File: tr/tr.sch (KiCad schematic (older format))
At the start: 104 parts, among them J1 SMA, J2 SMA, J3 SMA, K1 CONN_3, Q1 Si7850, Q3 STD2NK90ZT4, Q4 STD2NK90ZT4, T1 DA2033-AL_, U1 L6388E, U2 LT1631, U3 LT3757

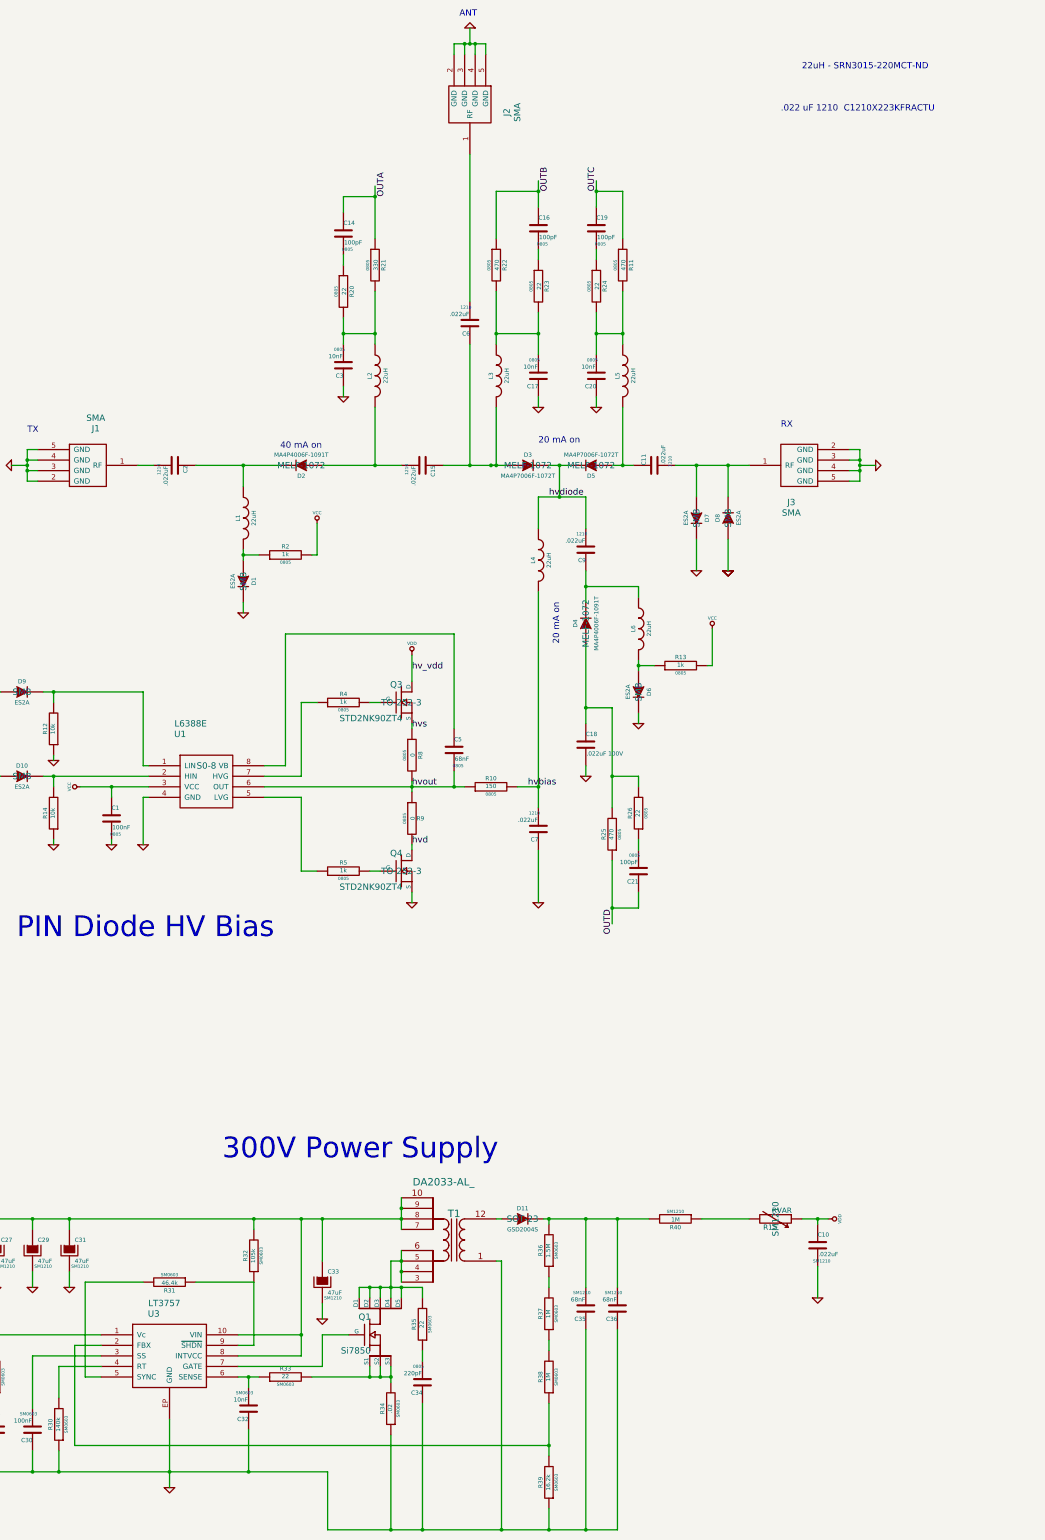
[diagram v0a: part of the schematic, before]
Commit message: routing for high voltage power supply
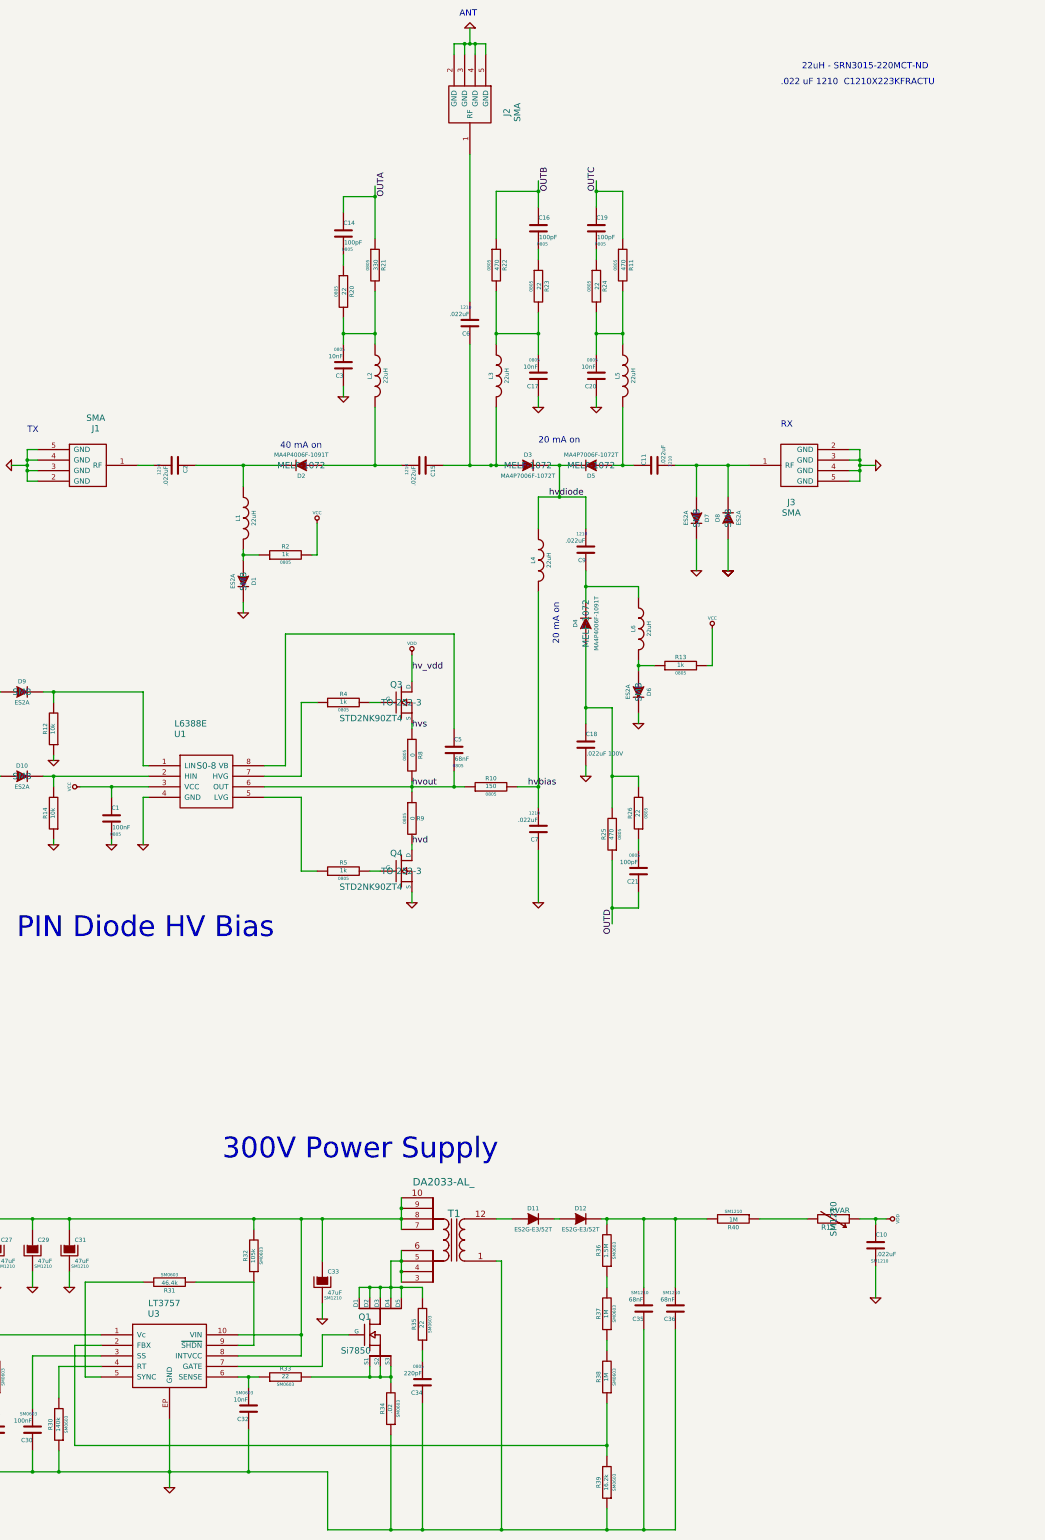
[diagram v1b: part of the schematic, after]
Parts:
- added D12: ES2G-E3/52T, ~, symbol DIODE
- D11: value GSD2004S -> ES2G-E3/52T; footprint SOT-23 -> ~
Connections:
- wire segments 255 -> 256
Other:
- moved on the sheet: C10, C35, C36, R15, R36, R37, R38, R39, R40

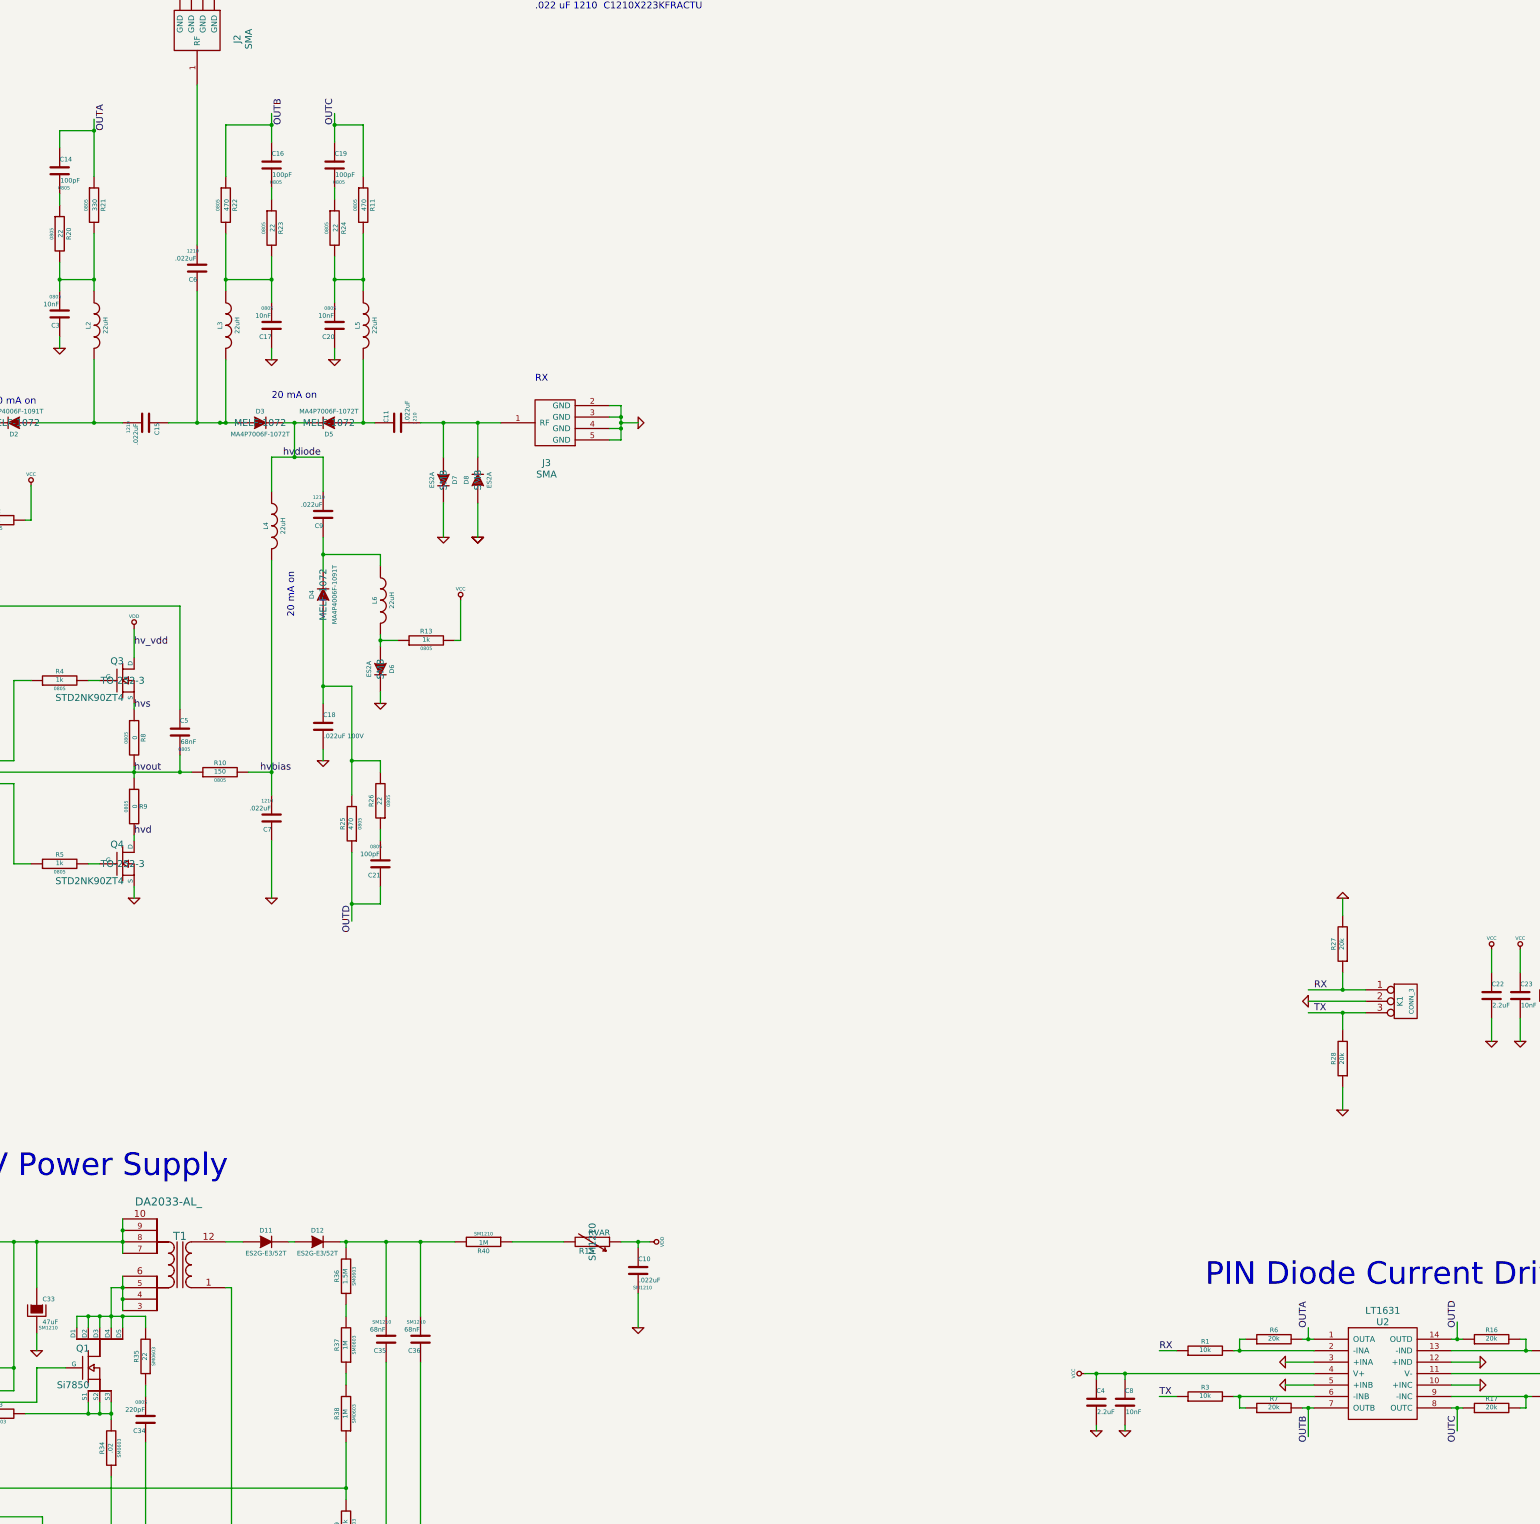
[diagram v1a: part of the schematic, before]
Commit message: work on transmitter layout
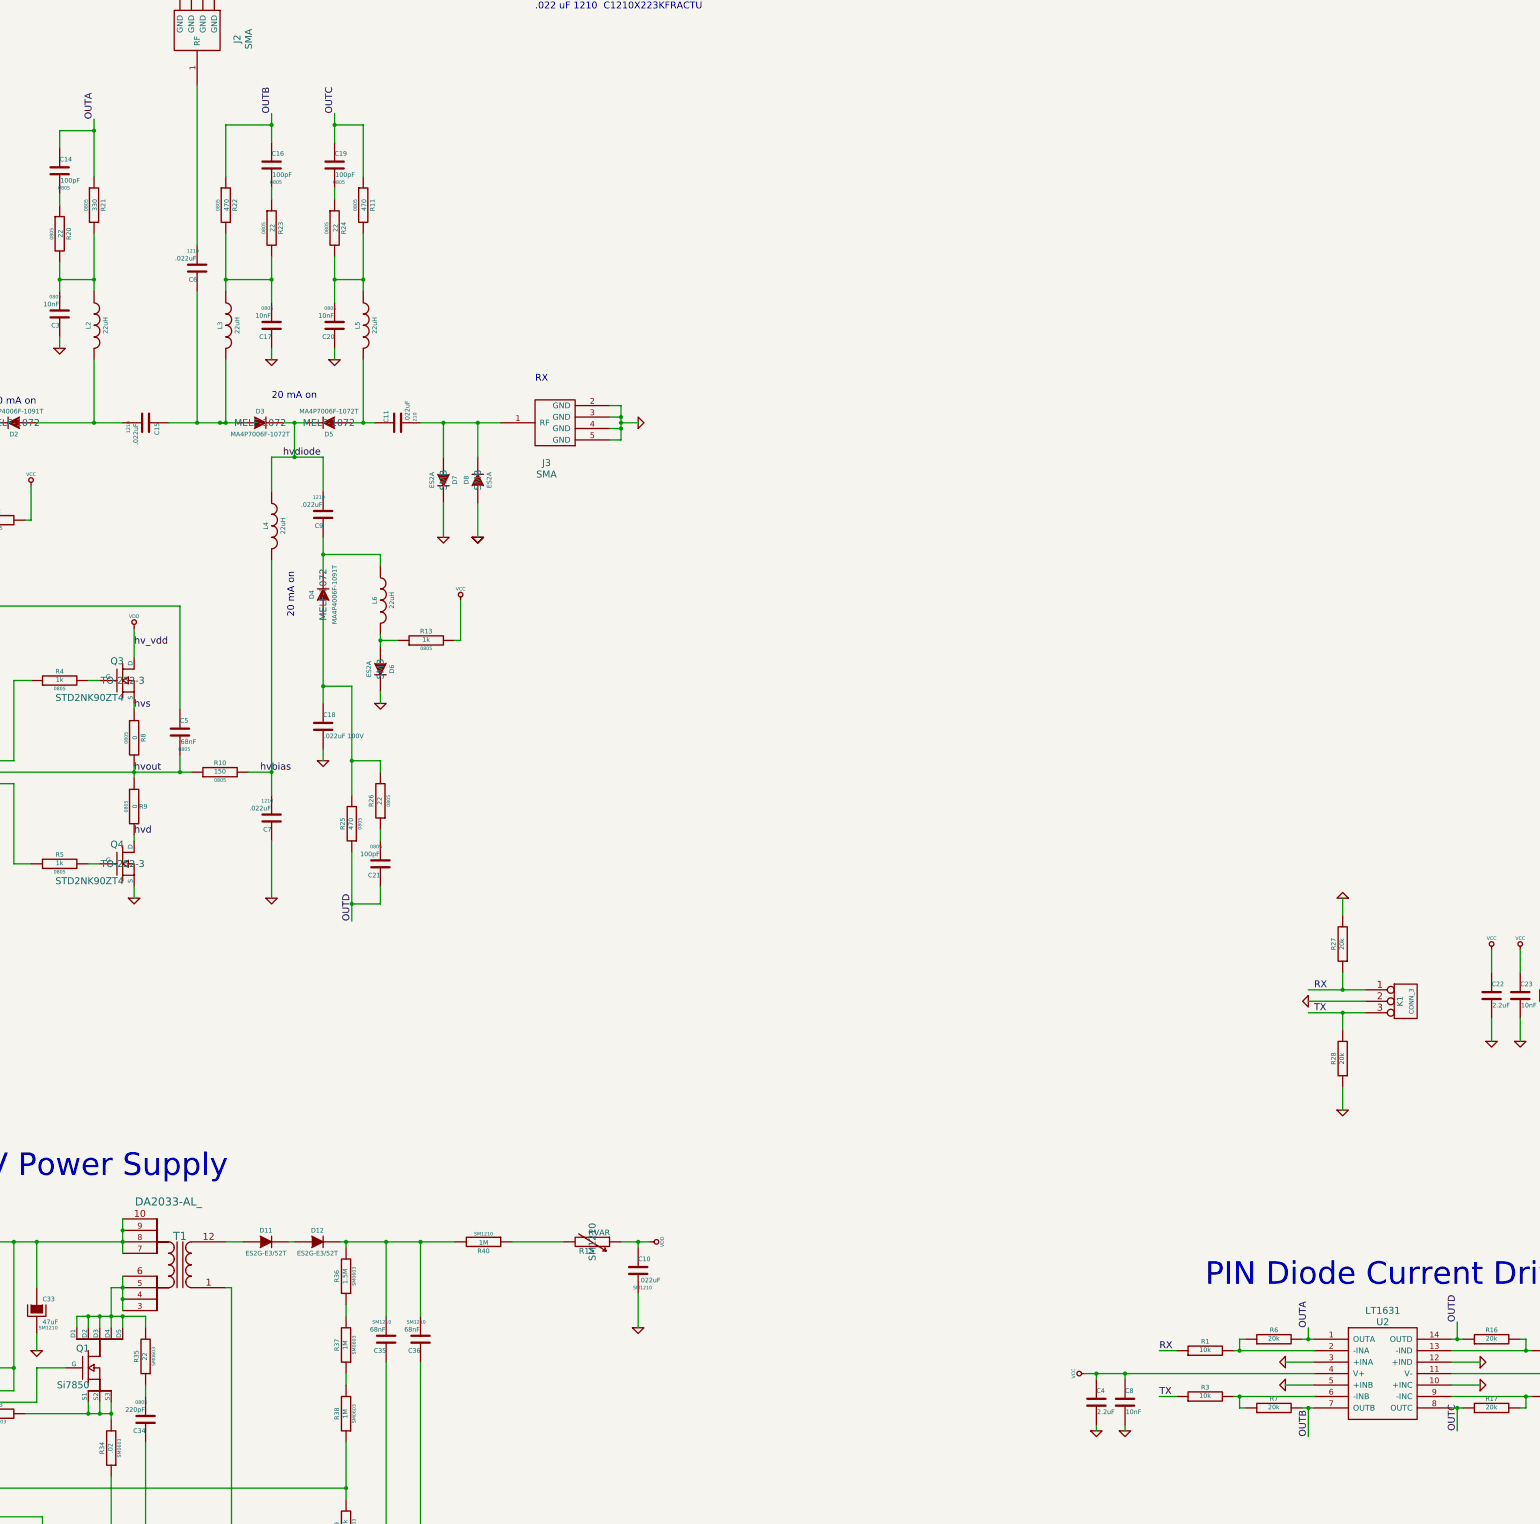
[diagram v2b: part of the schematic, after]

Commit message: added notes to schematic
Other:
- note added: "replace with 634U?\n"
- note added: "todo: optocouple inputs? isolate power supply? overdesign other aspects?"
- note removed: ".022 uF 1210 C1210X223KFRACTU"
- note removed: "22uH - SRN3015-220MCT-ND"
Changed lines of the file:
@@
 LIBS:transfo_multi
 LIBS:tr-cache
-EELAYER 27 0
+EELAYER 24 0
 EELAYER END
 $Descr C 22000 17000
@@
 Text Label 17250 10750 0    60   ~ 0
 TX
-Text Notes 10650 1850 0    60   ~ 0
-22uH - SRN3015-220MCT-ND
 $Comp
 L C C15
@@
 	1    0    0    -1
 $EndComp
-Text Notes 10450 2000 0    60   ~ 0
-.022 uF 1210  C1210X223KFRACTU
 Text Notes 5700 5450 0    60   ~ 0
 40 mA on\n
@@
 Wire Wire Line
 	8300 12750 8350 12750
+Text Notes 16950 12800 0    60   ~ 0
+replace with 634U?\n
+Text Notes 3100 10550 0    60   ~ 0
+todo: optocouple inputs? isolate power supply? overdesign other aspects?
 $EndSCHEMATC
